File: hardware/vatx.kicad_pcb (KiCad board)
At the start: 2 copper layers, 100 x 100 mm, 27 parts, among them J1 USB, P1 ATX, P10 CONN_1, P11 CONN_1, P2 CONN_1, P3 CONN_1, P4 CONN_1, P5 CONN_1, P6 CONN_1, P7 CONN_1, P8 CONN_1, P9 CONN_1, SW1 SWITCH_INV, U1 LM317T

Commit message: Add fabrications files/pdf
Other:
- board text added: "https://github.com/jerome-labidurie/vatx CC:BY-SA"
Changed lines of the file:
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@@
     (links 55)
     (no_connects 0)
-    (area 79.924999 49.924999 180.075001 150.075001)
+    (area 82.078736 25.35 198.075001 135.475001)
     (thickness 1.6)
-    (drawings 17)
+    (drawings 18)
     (tracks 104)
     (zones 0)
@@
     (pcbplotparams
       (layerselection 3178497)
-      (usegerberextensions true)
+      (usegerberextensions false)
       (excludeedgelayer true)
       (linewidth 0.150000)
       (plotframeref false)
-      (viasonmask false)
+      (viasonmask true)
       (mode 1)
       (useauxorigin false)
@@
       (outputformat 1)
       (mirror false)
-      (drillshape 1)
+      (drillshape 0)
       (scaleselection 1)
-      (outputdirectory ""))
+      (outputdirectory fabrication/))
   )
   (net 0 "")
@@
       (effects (font (thickness 0.3048)))
     )
-    (fp_text value ATX (at -0.2 -6.6) (layer F.SilkS)
+    (fp_text value ATX (at -23.2 0 90) (layer F.SilkS)
       (effects (font (thickness 0.3048)))
     )
@@
     (fp_line (start -1.99898 -23.50008) (end -1.09982 -21.20138) (layer B.Cu) (width 0.381))
   )
+  (gr_text "https://github.com/jerome-labidurie/vatx\nCC:BY-SA" (at 99.2 39.6) (layer F.SilkS)
+    (effects (font (size 1.5 1.5) (thickness 0.3) italic) (justify left))
+  )
   (gr_line (start 171.4 64.8) (end 129.6 64.8) (angle 90) (layer F.SilkS) (width 0.2))

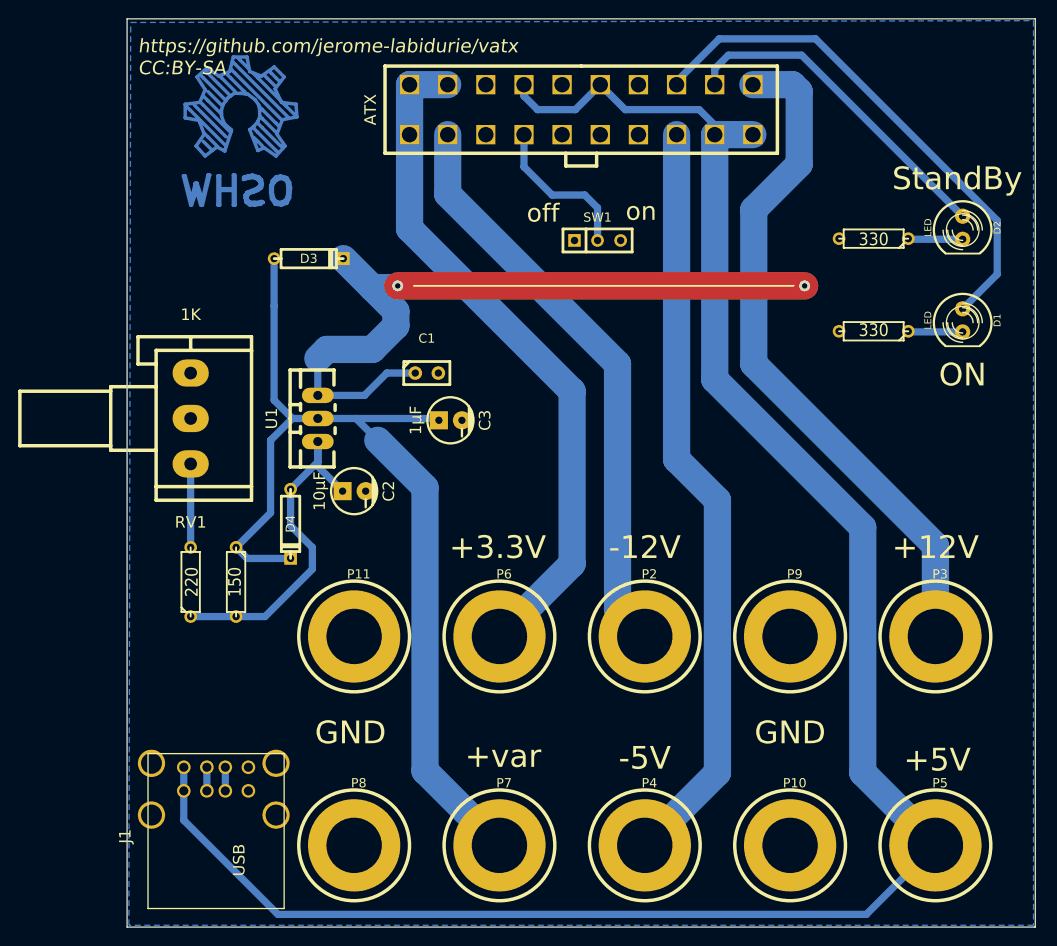
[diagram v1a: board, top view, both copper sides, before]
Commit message: Mounting holes
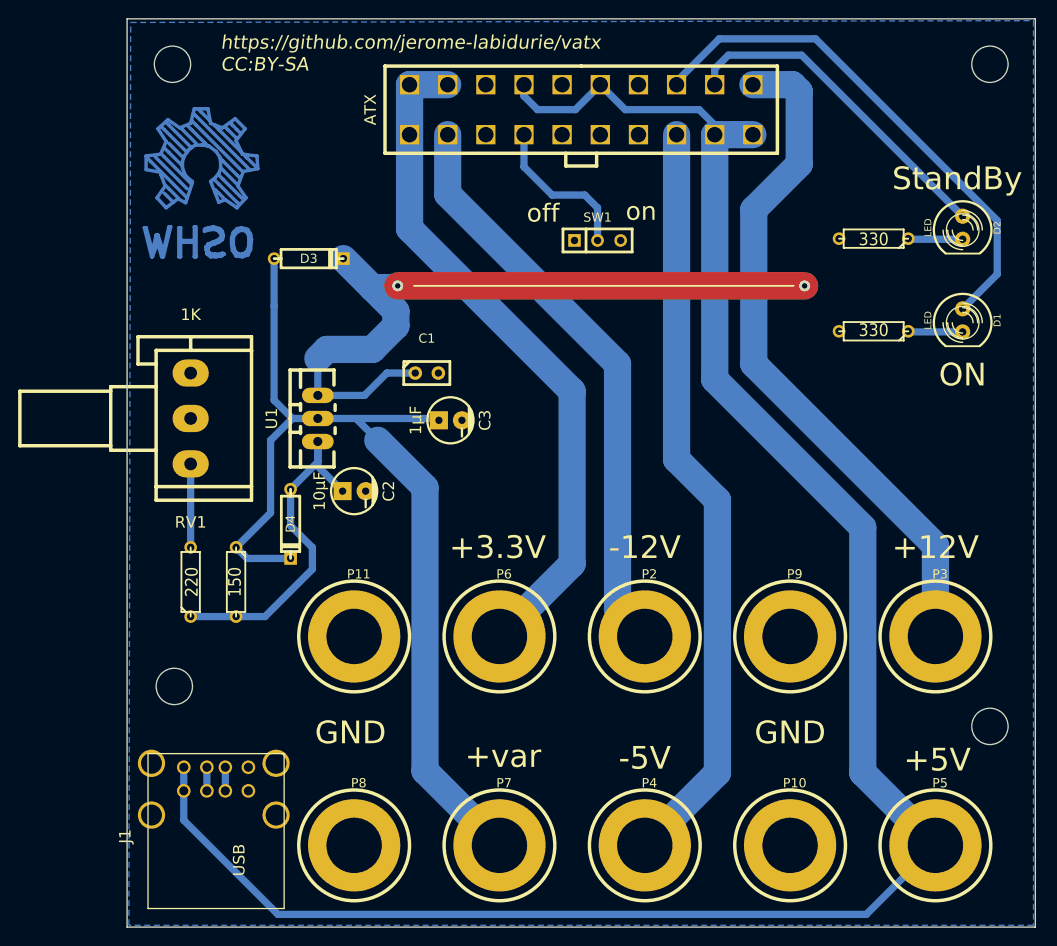
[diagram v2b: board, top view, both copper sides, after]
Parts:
- added MH: MountingHole_4mm_RevA_Date21Jun2010, Mounting_Holes:MountingHole_4mm, F.Cu at (193.0, 40.4)
- added MH: MountingHole_4mm_RevA_Date21Jun2010, Mounting_Holes:MountingHole_4mm, F.Cu at (193.0, 113.3)
- added MH: MountingHole_4mm_RevA_Date21Jun2010, Mounting_Holes:MountingHole_4mm, F.Cu at (103.2, 108.9)
- added MH: MountingHole_4mm_RevA_Date21Jun2010, Mounting_Holes:MountingHole_4mm, F.Cu at (103.0, 40.4)
- moved Sym 7.14 mm to (106.1, 32.1)

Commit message: Move to a smaller board * remove load resistor * remove -5 / -12 * 50x50mm pcb * SMD components for seeedstudio OPL
TODO:
* switch footprint
* check diodes footprint
* silkscreen
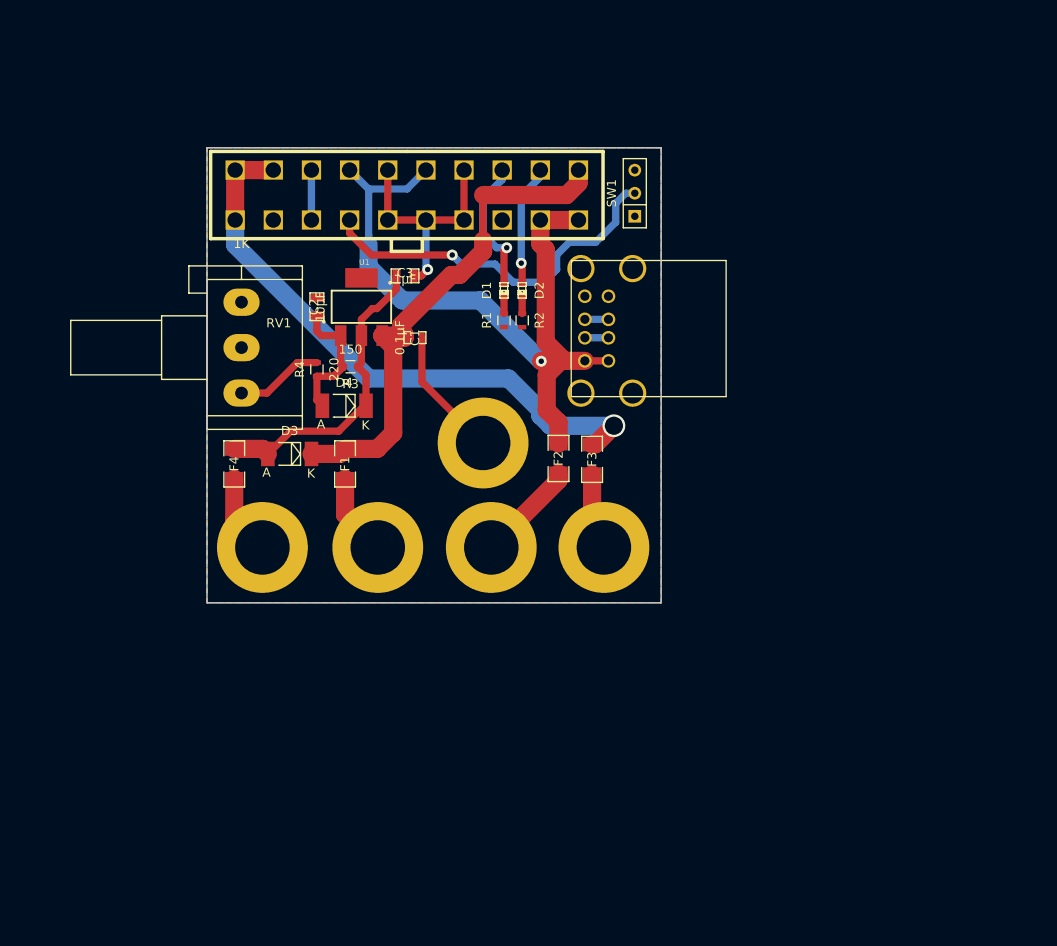
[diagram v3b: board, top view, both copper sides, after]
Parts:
- removed MH (x4): MountingHole_4mm_RevA_Date21Jun2010, Mounting_Holes:MountingHole_4mm
- removed P10, P11, P2, P8, P9: CONN_1, Iut:1PIN_6mm
- removed Sym: Symbol_OSHW-Logo_CopperTop_BIG_07Jul2012, Footprint_Symbols:Symbol_OSHW-Logo_CopperTop_BIG
- added F1: FUSE, SMD_Packages:SMD-1206, F.Cu at (122.0, 84.4)
- added F2: FUSE, SMD_Packages:SMD-1206, F.Cu at (145.5, 83.8)
- added F3: FUSE, SMD_Packages:SMD-1206, F.Cu at (149.2, 83.9)
- added F4: FUSE, SMD_Packages:SMD-1206, F.Cu at (109.8, 84.4)
- C1: footprint Capacitors:cnp_3mm_disc -> SMD_Packages:SMD-0603_c
- C2, C3: footprint Capacitors:CP_5x6mm -> SMD_Packages:SMD-0805
- D1, D2: footprint LEDs:LED-5MM -> LEDs:LED-0603
- D3, D4: value 1N4001 -> 1N4007; footprint Discret:D3 -> Diodes_SMD:Diode-MELF_Standard
- P1: value ATX -> CONN_10X2
- P3, P4, P5, P6, P7: footprint Iut:1PIN_6mm -> atx:Banana_single_6mmDrill
- R1, R2, R3, R4: footprint Discret:R3 -> Resistors_SMD:R_0603
- U1: footprint Transistors_TO-220:TO-220_Neutral123_Vertical_LargePads -> opl:SOT223
- moved J1 66.8 mm to (151.0, 69.5), turned to 0 degrees
- moved P3 62.2 mm to (125.6, 93.6)
- moved D1 50.6 mm to (139.5, 65.3)
- moved P5 49.1 mm to (150.5, 93.6)
- moved D2 49.0 mm to (141.5, 65.3)
- moved P7 44.3 mm to (137.2, 82.1)
- moved R1 40.7 mm to (139.5, 68.6), turned to 270 degrees
- moved R2 39.7 mm to (141.5, 68.6), turned to 270 degrees
- moved P4 36.9 mm to (138.1, 93.6)
- moved P6 27.9 mm to (112.9, 93.6)
- moved R4 27.2 mm to (118.9, 74.0)
- moved R3 26.8 mm to (122.6, 73.7), turned to 180 degrees
- moved D3 21.6 mm to (115.9, 83.3)
- moved P1 21.4 mm to (128.8, 54.8)
- moved C2 20.7 mm to (118.9, 67.1), turned to 90 degrees
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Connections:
- P3 pad 1: +12V -> f+12V
- P4 pad 1: -5V -> f+5V
- P5 pad 1: +5V -> f+3.3V
- P6 pad 1: +3.3V -> f+VAR
- P7 pad 1: +VAR -> GND
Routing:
- net +5V: track 215.5 -> 81.1 mm, vias 0 -> 1
- net +12V: track 164.7 -> 58.6 mm, vias 2 -> 0
- net -5V: track 83.4 -> 0.00 mm
- net +VAR: track 111.5 -> 34.5 mm
- net -12V: track 64.2 -> 0.00 mm
- net GND: track 0.00 -> 46.7 mm, vias 0 -> 1
- net POK: track 57.2 -> 15.2 mm, vias 0 -> 1
- net PSON: track 17.1 -> 41.3 mm, vias 0 -> 1
- net +5VSB: track 37.0 -> 13.4 mm, vias 0 -> 1
- net Net-(C2-Pad1): track 38.4 -> 15.0 mm
- net f+VAR: track 0.00 -> 13.2 mm
- net f+5V: track 0.00 -> 11.2 mm
- net f+3.3V: track 0.00 -> 10.4 mm
- net +3.3V: track 75.7 -> 66.0 mm, vias 0 -> 1
- net f+12V: track 0.00 -> 9.04 mm
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- added copper zone on F.Cu, net GND
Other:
- board size 100 x 100 mm -> 50 x 50.1 mm
- net class Default: clearance 0.8 -> 0.5
- rule trace_clearance: 0.8 -> 0.5
- board text removed: "+12V"
- board text removed: "+3.3V"
- board text removed: "+5V"
- board text removed: "+var"
- board text removed: "-12V"
- board text removed: "-5V"
- board text removed: "GND"
- board text removed: "ON"
- board text removed: "StandBy"
- board text removed: "https://github.com/jerome-labidurie/vatx CC:BY-SA"
- board text removed: "off"
- board text removed: "on"

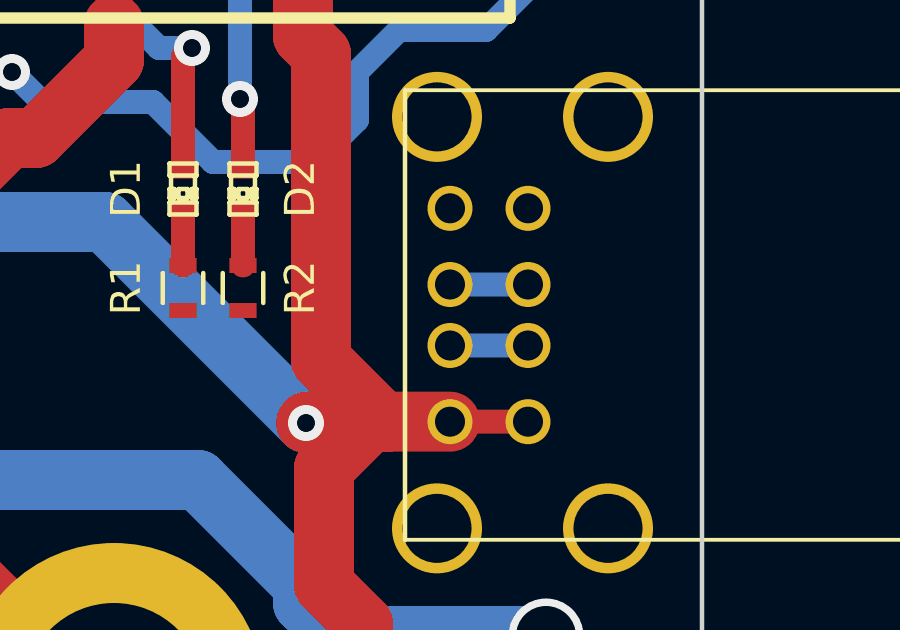
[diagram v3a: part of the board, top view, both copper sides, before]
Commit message: Short between D+/D- to be an USB DCP http://www.maximintegrated.com/en/app-notes/index.mvp/id/4803
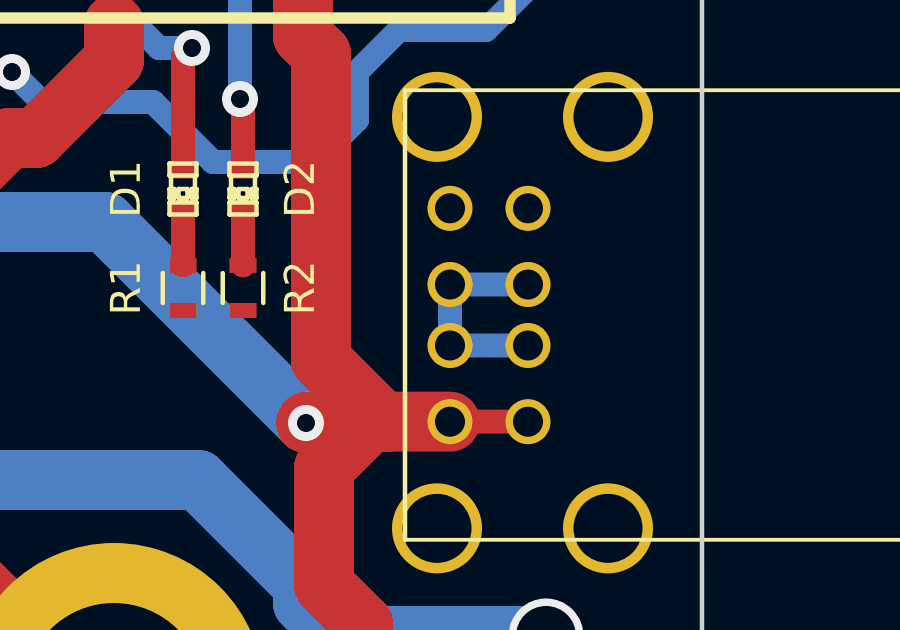
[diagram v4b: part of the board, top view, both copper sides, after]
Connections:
- J1 pad 3: Net-(J1-Pad3) -> Net-(J1-Pad2)
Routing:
- net Net-(J1-Pad2): track 2.60 -> 7.23 mm
- net Net-(J1-Pad3): track 2.60 -> 0.00 mm

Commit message: Silkscreen
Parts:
- added Symbol_OSHW-Logo_SilkScreen: VAL**, Footprint_Symbols:Symbol_OSHW-Logo_SilkScreen, F.Cu at (133.9, 68.7)
- added Symbol_OSHW-Logo_SilkScreen_BIG: VAL**, Footprint_Symbols:Symbol_OSHW-Logo_SilkScreen_BIG, B.Cu at (125.1, 50.4)
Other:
- board text added: "12V"
- board text added: "3.3V"
- board text added: "5V"
- board text added: "GND"
- board text added: "VAR"
- board text added: "http://fablab-lannion.org/wiki/index.php?title=VATX dinask.eu"

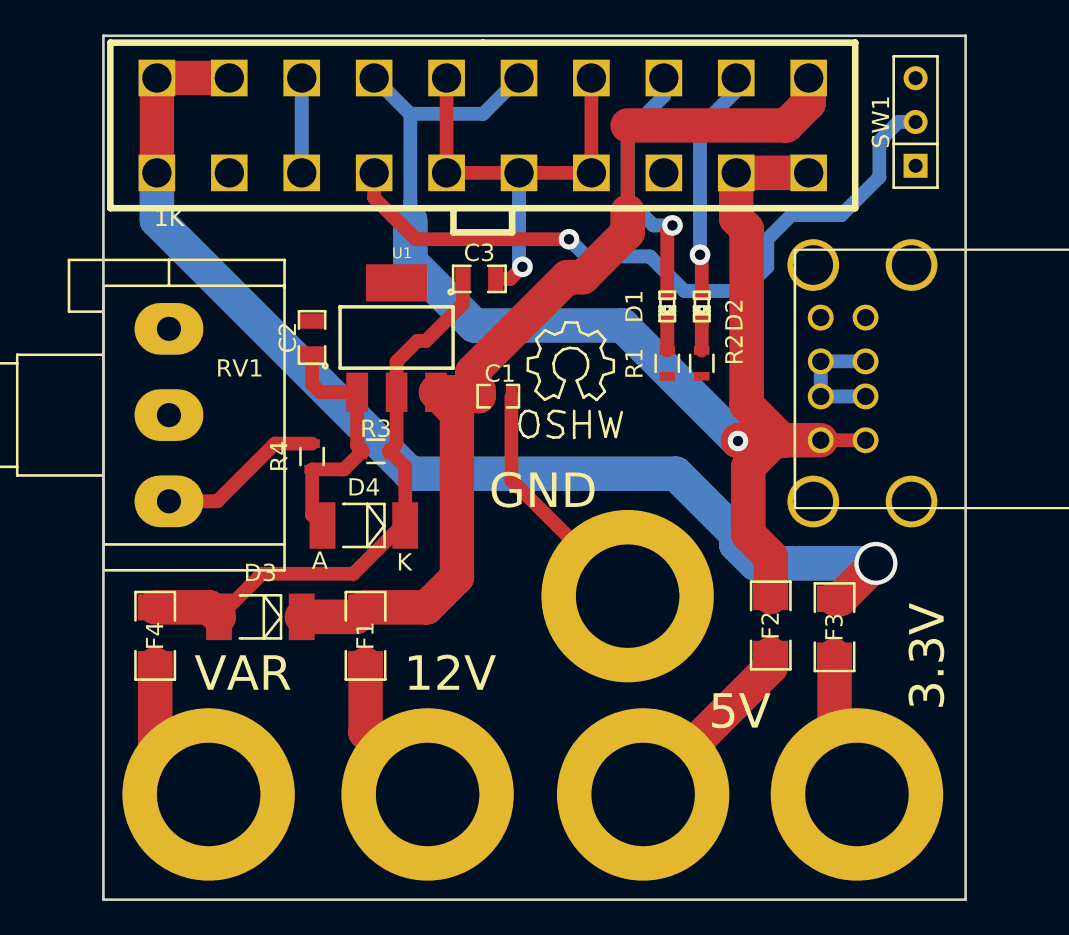
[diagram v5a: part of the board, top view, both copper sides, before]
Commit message: LM317 heatsink
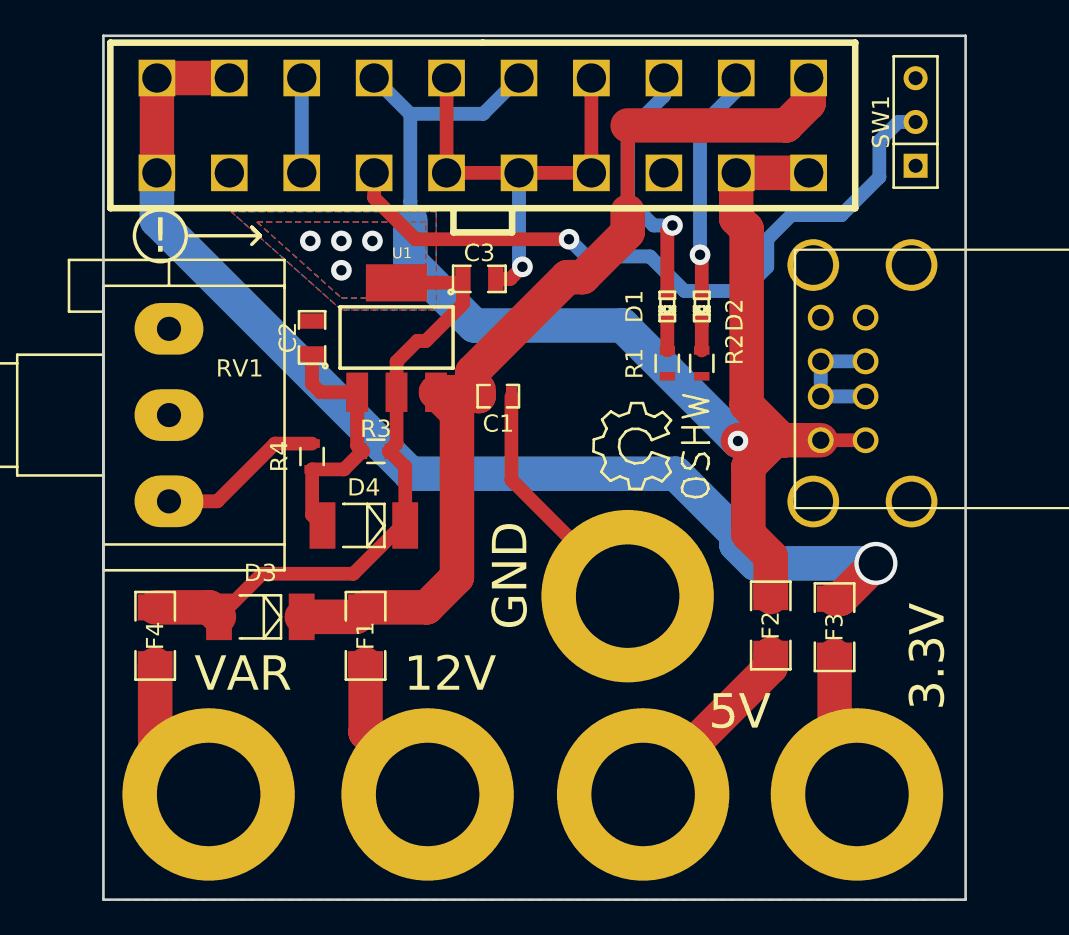
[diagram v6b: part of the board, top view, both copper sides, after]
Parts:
- moved Symbol_OSHW-Logo_SilkScreen 6.04 mm to (137.7, 73.4), turned to 90 degrees
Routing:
- net +VAR: track 34.5 -> 38.4 mm
- net (no net): vias 0 -> 4
- added copper zone on B.Cu, net +VAR
- added copper zone on F.Cu, net +VAR
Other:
- board text added: "!"
